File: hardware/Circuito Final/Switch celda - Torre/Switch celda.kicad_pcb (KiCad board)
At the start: 2 copper layers, 100 x 40 mm, 30 parts, among them Q1 MMBT2222A, Q2 MMBT2907A, Q3 MMBT2222A

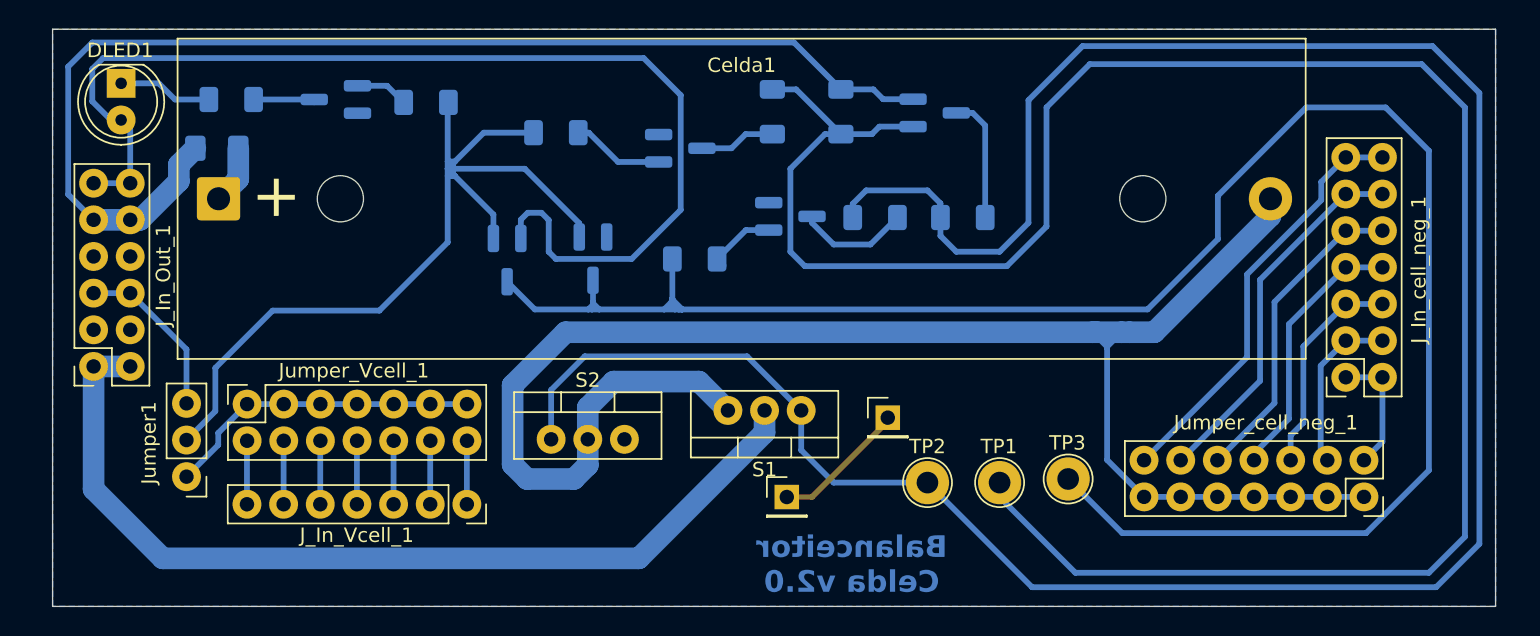
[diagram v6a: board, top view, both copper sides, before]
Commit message: Eliminación del pin de señal de control para todo el banco y correcciones menores a la placa
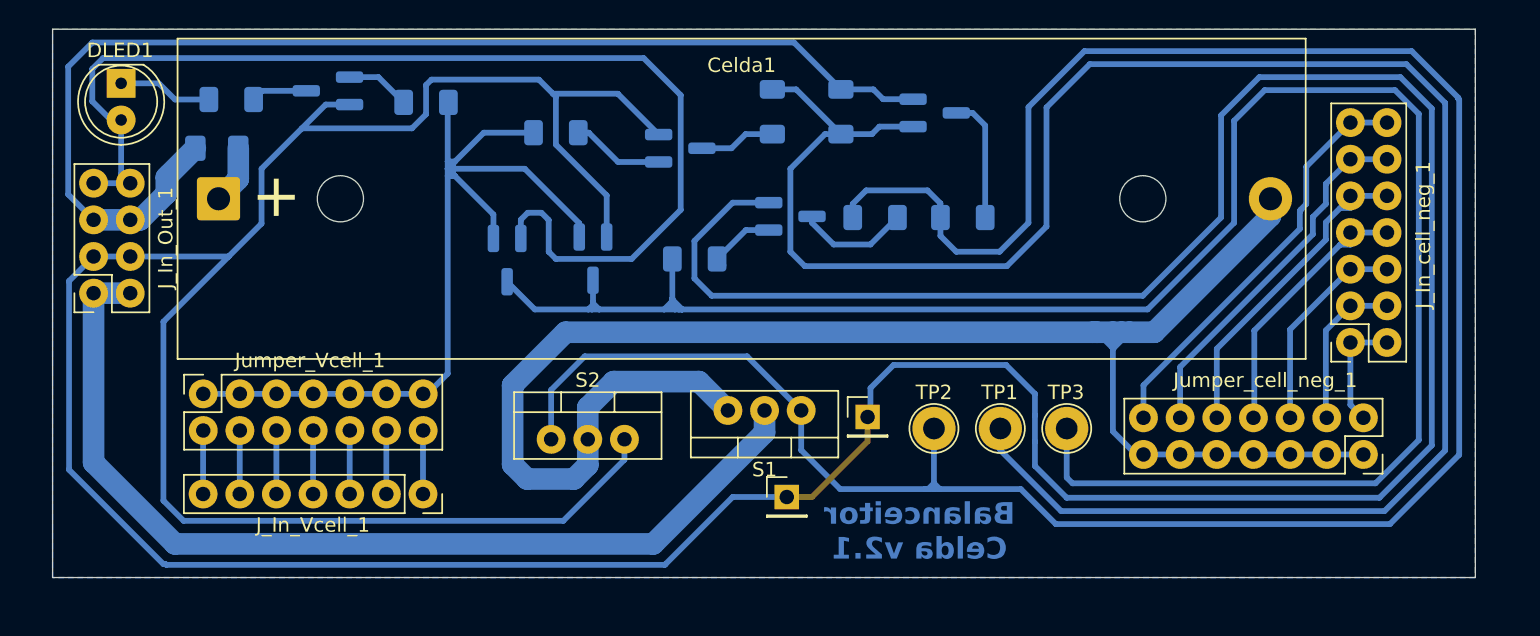
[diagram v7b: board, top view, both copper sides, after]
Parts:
- removed Jumper1: Conn_01x03_Pin, Connector_PinHeader_2.54mm:PinHeader_1x03_P2.54mm_Vertical
- J_In_Out_1: value Conn_02x06_Odd_Even -> Conn_02x04_Odd_Even; footprint Connector_PinSocket_2.54mm:PinSocket_2x06_P2.54mm_Vertical -> Connector_PinSocket_2.54mm:PinSocket_2x04_P2.54mm_Vertical
- moved J_In_Out_1 5.08 mm to (103.0, 102.6)
- moved TP2 3.78 mm to (161.2, 112.0)
- moved TP1 3.75 mm to (165.8, 112.0)
- moved TP3 3.50 mm to (170.4, 112.0)
- moved J_In_Vcell_1 3.12 mm to (125.8, 116.5)
- moved Jumper_Vcell_1 3.12 mm to (110.6, 109.6)
- moved Jumper_cell_neg_1 2.94 mm to (191.0, 113.8)
- moved J_In_cell_neg_1 2.43 mm to (190.1, 106.0)
- moved TPgnd1 1.40 mm to (156.6, 111.2)
- moved QLED1 0.81 mm to (119.2, 88.6)
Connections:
- J_In_Out_1 pad 5: Vcell_banco -> bus_pos
- J_In_Out_1 pad 6: Vcell_banco -> bus_pos
- J_In_Out_1 pad 7: 0 -> Vcc
- J_In_Out_1 pad 8: 0 -> Vcc
- Qinv1 pad 2: Vin -> Vcell
- Qinv2 pad 2: Vin -> Vcell
- R1 pad 1: Vin -> Vcell
- RLED1 pad 1: Vin -> Vcell
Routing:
- net 0: track 9.42 -> 343.0 mm
- net Vin: track 63.1 -> 0.00 mm
- net Vcell: track 22.0 -> 64.2 mm
- net Vcell_banco: track 11.8 -> 0.00 mm
- net Net-(Q2-B): track 146.7 -> 138.9 mm
- net Net-(S1-G): track 169.5 -> 164.2 mm
- net bus_neg: track 64.7 -> 67.8 mm
- net Net-(Qinv1-D): track 133.6 -> 136.5 mm
- net Vcell_neg: track 116.0 -> 113.4 mm
- net Net-(QLED1-B): track 3.68 -> 4.47 mm
- net cell_neg2: track 11.7 -> 11.0 mm
- net cell_neg1: track 8.82 -> 8.13 mm
- net Net-(QLED1-C): track 4.48 -> 3.90 mm
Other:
- board size 100 x 40 mm -> 98.6 x 38 mm
- board text added: "Balanceitor Celda v2.1"
- board text removed: "Balanceitor Celda v2.0"

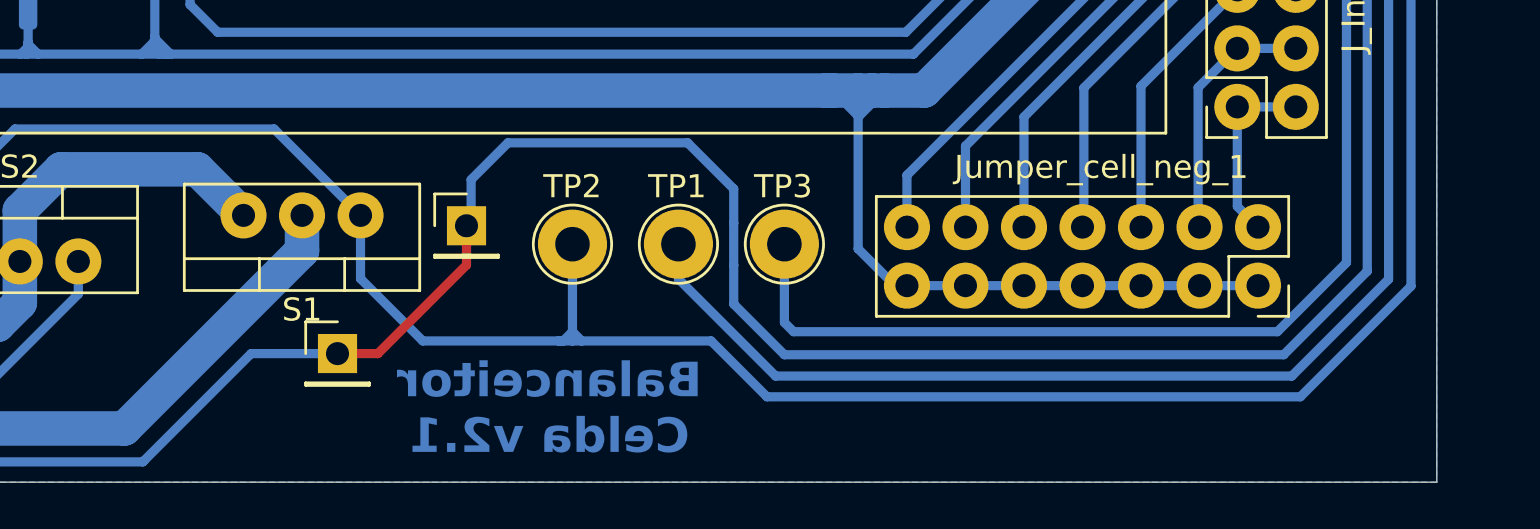
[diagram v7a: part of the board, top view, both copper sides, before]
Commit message: Reemplazo de la vía por un resistor SMD de 0 ohm y corrección de los errores de DRC
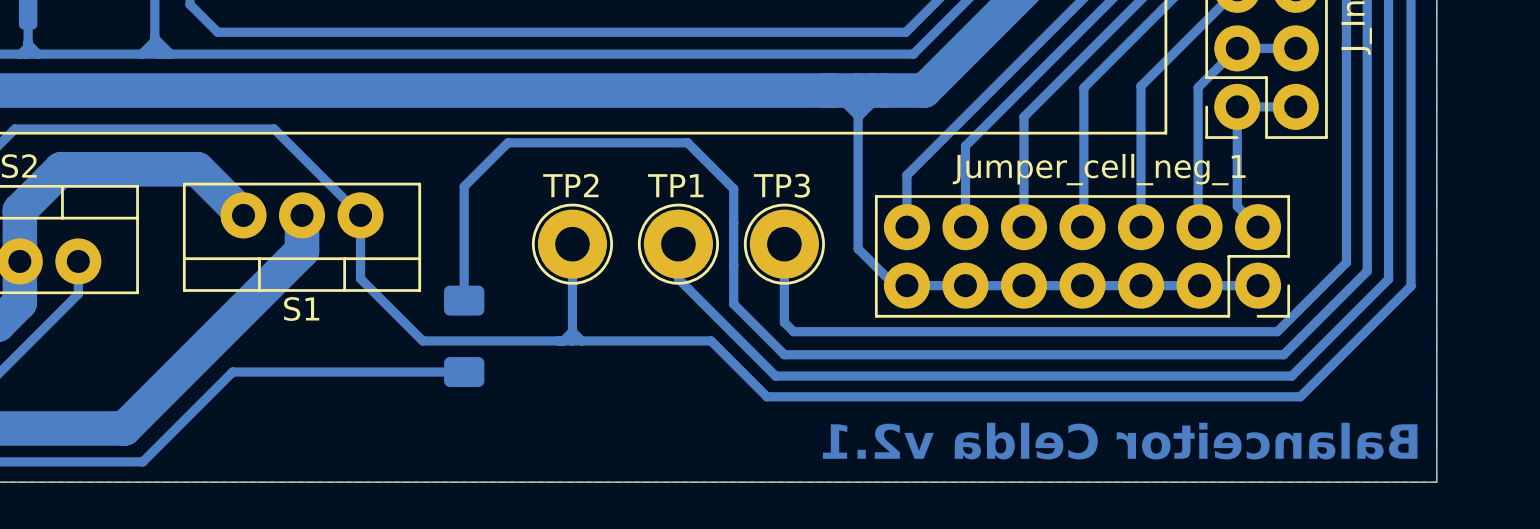
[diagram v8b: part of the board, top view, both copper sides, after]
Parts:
- removed TPgnd1, TPgnd2: TP_gnd, Connector_PinHeader_2.54mm:PinHeader_1x01_P2.54mm_Vertical
- added Rvia1: 0, Resistor_SMD:R_1206_3216Metric_Pad1.30x1.75mm_HandSolder, B.Cu at (156.5, 116.0)
